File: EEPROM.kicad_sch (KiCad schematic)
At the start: 22 parts, among them IC1 PCA6408APW, IC2 AT24CS01, U2 TPS613221ADBVT

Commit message: Update signage
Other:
- moved on the sheet: C34, C37, C38, C39, D1, D2, D3, D4, IC1, IC2, L1, R10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

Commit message: [#45231] globlib
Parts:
- C34, C37: footprint lpddr4-testbed-footprints:0402-cap -> antmicro-footprints:C_0402_1005Metric; symbol lpddr4-testbed:C_4u7_0402 -> antmicroCapacitors0402:C_4u7_0402
- C38, C39: footprint lpddr4-testbed-footprints:0402-cap -> antmicro-footprints:C_0402_1005Metric; symbol lpddr4-testbed:C_100n_0402 -> antmicroCapacitors0402:C_100n_0402
- R10, R11, R12, R9: footprint lpddr4-testbed-footprints:0402-res -> antmicro-footprints:R_0402_1005Metric; symbol lpddr4-testbed:R_220R_0402 -> antmicroResistors0402:R_220R_0402
- R13, R14: footprint lpddr4-testbed-footprints:0402-res -> antmicro-footprints:R_0402_1005Metric; symbol lpddr4-testbed:R_10k_0402 -> antmicroResistors0402:R_10k_0402
- R8: footprint lpddr4-testbed-footprints:0402-res -> antmicro-footprints:R_0402_1005Metric; symbol lpddr4-testbed:R_0R_0402 -> antmicroResistors0402:R_0R_0402
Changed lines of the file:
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@@
     )
   )
-  (symbol (lib_id "lpddr4-testbed:C_4u7_0402") (at 189.865 91.44 0) (unit 1)
+  (symbol (lib_id "antmicroCapacitors0402:C_4u7_0402") (at 189.865 91.44 0) (unit 1)
     (in_bom yes) (on_board yes)
     (property "Reference" "C34" (id 0) (at 192.786 90.297 0)
@@
       (effects (font (size 1.524 1.524)) hide)
     )
-    (property "Footprint" "lpddr4-testbed-footprints:0402-cap" (id 2) (at 194.945 86.36 0)
+    (property "Footprint" "antmicro-footprints:C_0402_1005Metric" (id 2) (at 194.945 86.36 0)
       (effects (font (size 1.524 1.524)) (justify left) hide)
     )
@@
     (pin "2")
   )
-  (symbol (lib_id "lpddr4-testbed:C_4u7_0402") (at 235.585 91.44 0) (unit 1)
+  (symbol (lib_id "antmicroCapacitors0402:C_4u7_0402") (at 235.585 91.44 0) (unit 1)
     (in_bom yes) (on_board yes)
     (property "Reference" "C37" (id 0) (at 238.506 90.297 0)
@@
       (effects (font (size 1.524 1.524)) hide)
     )
-    (property "Footprint" "lpddr4-testbed-footprints:0402-cap" (id 2) (at 240.665 86.36 0)
+    (property "Footprint" "antmicro-footprints:C_0402_1005Metric" (id 2) (at 240.665 86.36 0)
       (effects (font (size 1.524 1.524)) (justify left) hide)
     )
@@
     (pin "5")
   )
-  (symbol (lib_id "lpddr4-testbed:R_0R_0402") (at 212.725 76.2 0) (unit 1)
+  (symbol (lib_id "antmicroResistors0402:R_0R_0402") (at 212.725 76.2 0) (unit 1)
     (in_bom yes) (on_board yes)
     (property "Reference" "R8" (id 0) (at 212.725 71.12 0)
@@
       (effects (font (size 1.524 1.524)) hide)
     )
-    (property "Footprint" "lpddr4-testbed-footprints:0402-res" (id 2) (at 217.805 71.12 0)
+    (property "Footprint" "antmicro-footprints:R_0402_1005Metric" (id 2) (at 217.805 71.12 0)
       (effects (font (size 1.524 1.524)) (justify left) hide)
     )
@@
     (pin "2")
   )
-  (symbol (lib_id "lpddr4-testbed:GND") (at 189.865 95.25 0) (unit 1)
+  (symbol (lib_id "antmicropower:GND") (at 189.865 95.25 0) (unit 1)
     (in_bom yes) (on_board yes)
     (property "Reference" "#PWR0106" (id 0) (at 189.865 101.6 0)
@@
     (pin "1")
   )
-  (symbol (lib_id "lpddr4-testbed:GND") (at 235.585 95.25 0) (unit 1)
+  (symbol (lib_id "antmicropower:GND") (at 235.585 95.25 0) (unit 1)
     (in_bom yes) (on_board yes)
     (property "Reference" "#PWR0107" (id 0) (at 235.585 101.6 0)
@@
     (pin "1")
   )
-  (symbol (lib_id "lpddr4-testbed:GND") (at 230.505 95.25 0) (unit 1)
+  (symbol (lib_id "antmicropower:GND") (at 230.505 95.25 0) (unit 1)
     (in_bom yes) (on_board yes)
     (property "Reference" "#PWR0108" (id 0) (at 230.505 101.6 0)
@@
     (pin "1")
   )
-  (symbol (lib_id "lpddr4-testbed:R_10k_0402") (at 188.595 175.26 270) (unit 1)
+  (symbol (lib_id "antmicroResistors0402:R_10k_0402") (at 188.595 175.26 270) (unit 1)
     (in_bom yes) (on_board yes)
     (property "Reference" "R13" (id 0) (at 190.373 174.117 90)
@@
       (effects (font (size 1.524 1.524)) hide)
     )
-    (property "Footprint" "lpddr4-testbed-footprints:0402-res" (id 2) (at 193.675 180.34 0)
+    (property "Footprint" "antmicro-footprints:R_0402_1005Metric" (id 2) (at 193.675 180.34 0)
       (effects (font (size 1.524 1.524)) (justify left) hide)
     )
@@
     (pin "2")
   )
-  (symbol (lib_id "lpddr4-testbed:R_220R_0402") (at 248.285 120.65 0) (unit 1)
+  (symbol (lib_id "antmicroResistors0402:R_220R_0402") (at 248.285 120.65 0) (unit 1)
     (in_bom yes) (on_board yes)
     (property "Reference" "R9" (id 0) (at 243.205 119.38 0)
@@
       (effects (font (size 1.524 1.524)) hide)
     )
-    (property "Footprint" "lpddr4-testbed-footprints:0402-res" (id 2) (at 253.365 115.57 0)
+    (property "Footprint" "antmicro-footprints:R_0402_1005Metric" (id 2) (at 253.365 115.57 0)
       (effects (font (size 1.524 1.524)) (justify left) hide)
     )
@@
     (pin "2")
   )
-  (symbol (lib_id "lpddr4-testbed:R_220R_0402") (at 248.285 123.19 0) (unit 1)
+  (symbol (lib_id "antmicroResistors0402:R_220R_0402") (at 248.285 123.19 0) (unit 1)
     (in_bom yes) (on_board yes)
     (property "Reference" "R10" (id 0) (at 243.205 121.92 0)
@@
       (effects (font (size 1.524 1.524)) hide)
     )
-    (property "Footprint" "lpddr4-testbed-footprints:0402-res" (id 2) (at 253.365 118.11 0)
+    (property "Footprint" "antmicro-footprints:R_0402_1005Metric" (id 2) (at 253.365 118.11 0)
       (effects (font (size 1.524 1.524)) (justify left) hide)
     )
@@
     (pin "2")
   )
-  (symbol (lib_id "lpddr4-testbed:R_220R_0402") (at 248.285 125.73 0) (unit 1)
+  (symbol (lib_id "antmicroResistors0402:R_220R_0402") (at 248.285 125.73 0) (unit 1)
     (in_bom yes) (on_board yes)
     (property "Reference" "R11" (id 0) (at 243.205 124.46 0)
@@
       (effects (font (size 1.524 1.524)) hide)
     )
-    (property "Footprint" "lpddr4-testbed-footprints:0402-res" (id 2) (at 253.365 120.65 0)
+    (property "Footprint" "antmicro-footprints:R_0402_1005Metric" (id 2) (at 253.365 120.65 0)
       (effects (font (size 1.524 1.524)) (justify left) hide)
     )
@@
     (pin "2")
   )
-  (symbol (lib_id "lpddr4-testbed:R_220R_0402") (at 248.285 128.27 0) (unit 1)
+  (symbol (lib_id "antmicroResistors0402:R_220R_0402") (at 248.285 128.27 0) (unit 1)
     (in_bom yes) (on_board yes)
     (property "Reference" "R12" (id 0) (at 243.205 127 0)
@@
       (effects (font (size 1.524 1.524)) hide)
     )
-    (property "Footprint" "lpddr4-testbed-footprints:0402-res" (id 2) (at 253.365 123.19 0)
+    (property "Footprint" "antmicro-footprints:R_0402_1005Metric" (id 2) (at 253.365 123.19 0)
       (effects (font (size 1.524 1.524)) (justify left) hide)
     )
@@
     (pin "2")
   )
-  (symbol (lib_id "lpddr4-testbed:C_100n_0402") (at 253.365 182.88 0) (unit 1)
+  (symbol (lib_id "antmicroCapacitors0402:C_100n_0402") (at 253.365 182.88 0) (unit 1)
     (in_bom yes) (on_board yes)
     (property "Reference" "C38" (id 0) (at 256.286 181.737 0)
@@
       (effects (font (size 1.524 1.524)) hide)
     )
-    (property "Footprint" "lpddr4-testbed-footprints:0402-cap" (id 2) (at 258.445 177.8 0)
+    (property "Footprint" "antmicro-footprints:C_0402_1005Metric" (id 2) (at 258.445 177.8 0)
       (effects (font (size 1.524 1.524)) (justify left) hide)
     )
@@
     (pin "2")
   )
-  (symbol (lib_id "lpddr4-testbed:GND") (at 258.445 153.67 0) (unit 1)
+  (symbol (lib_id "antmicropower:GND") (at 258.445 153.67 0) (unit 1)
     (in_bom yes) (on_board yes)
     (property "Reference" "#PWR0109" (id 0) (at 258.445 160.02 0)
@@
     (pin "1")
   )
-  (symbol (lib_id "lpddr4-testbed:GND") (at 266.065 153.67 0) (unit 1)
+  (symbol (lib_id "antmicropower:GND") (at 266.065 153.67 0) (unit 1)
     (in_bom yes) (on_board yes)
     (property "Reference" "#PWR0110" (id 0) (at 266.065 160.02 0)
@@
     (pin "1")
   )
-  (symbol (lib_id "lpddr4-testbed:GND") (at 273.685 153.67 0) (unit 1)
+  (symbol (lib_id "antmicropower:GND") (at 273.685 153.67 0) (unit 1)
     (in_bom yes) (on_board yes)
     (property "Reference" "#PWR0111" (id 0) (at 273.685 160.02 0)
@@
     (pin "1")
   )
-  (symbol (lib_id "lpddr4-testbed:GND") (at 281.305 153.67 0) (unit 1)
+  (symbol (lib_id "antmicropower:GND") (at 281.305 153.67 0) (unit 1)
     (in_bom yes) (on_board yes)
     (property "Reference" "#PWR0112" (id 0) (at 281.305 160.02 0)
@@
     (pin "1")
   )
-  (symbol (lib_id "lpddr4-testbed:GND") (at 198.755 152.4 0) (unit 1)
+  (symbol (lib_id "antmicropower:GND") (at 198.755 152.4 0) (unit 1)
     (in_bom yes) (on_board yes)
     (property "Reference" "#PWR0113" (id 0) (at 198.755 158.75 0)
@@
     (pin "5")
   )
-  (symbol (lib_id "lpddr4-testbed:R_10k_0402") (at 196.215 175.26 270) (unit 1)
+  (symbol (lib_id "antmicroResistors0402:R_10k_0402") (at 196.215 175.26 270) (unit 1)
     (in_bom yes) (on_board yes)
     (property "Reference" "R14" (id 0) (at 197.993 174.117 90)
@@
       (effects (font (size 1.524 1.524)) hide)
     )
-    (property "Footprint" "lpddr4-testbed-footprints:0402-res" (id 2) (at 201.295 180.34 0)
+    (property "Footprint" "antmicro-footprints:R_0402_1005Metric" (id 2) (at 201.295 180.34 0)
       (effects (font (size 1.524 1.524)) (justify left) hide)
     )
@@
     (pin "2")
   )
-  (symbol (lib_id "lpddr4-testbed:GND") (at 196.215 190.5 0) (unit 1)
+  (symbol (lib_id "antmicropower:GND") (at 196.215 190.5 0) (unit 1)
     (in_bom yes) (on_board yes)
     (property "Reference" "#PWR0114" (id 0) (at 196.215 196.85 0)
@@
     (pin "1")
   )
-  (symbol (lib_id "lpddr4-testbed:GND") (at 231.775 190.5 0) (unit 1)
+  (symbol (lib_id "antmicropower:GND") (at 231.775 190.5 0) (unit 1)
     (in_bom yes) (on_board yes)
     (property "Reference" "#PWR0115" (id 0) (at 231.775 196.85 0)
@@
     (pin "1")
   )
-  (symbol (lib_id "lpddr4-testbed:GND") (at 253.365 190.5 0) (unit 1)
+  (symbol (lib_id "antmicropower:GND") (at 253.365 190.5 0) (unit 1)
     (in_bom yes) (on_board yes)
     (property "Reference" "#PWR0116" (id 0) (at 253.365 196.85 0)
@@
     (pin "1")
   )
-  (symbol (lib_id "lpddr4-testbed:C_100n_0402") (at 266.065 182.88 0) (unit 1)
+  (symbol (lib_id "antmicroCapacitors0402:C_100n_0402") (at 266.065 182.88 0) (unit 1)
     (in_bom yes) (on_board yes)
     (property "Reference" "C39" (id 0) (at 268.986 181.737 0)
@@
       (effects (font (size 1.524 1.524)) hide)
     )
-    (property "Footprint" "lpddr4-testbed-footprints:0402-cap" (id 2) (at 271.145 177.8 0)
+    (property "Footprint" "antmicro-footprints:C_0402_1005Metric" (id 2) (at 271.145 177.8 0)
       (effects (font (size 1.524 1.524)) (justify left) hide)
     )
@@
     (pin "2")
   )
-  (symbol (lib_id "lpddr4-testbed:GND") (at 266.065 190.5 0) (unit 1)
+  (symbol (lib_id "antmicropower:GND") (at 266.065 190.5 0) (unit 1)
     (in_bom yes) (on_board yes)
     (property "Reference" "#PWR0117" (id 0) (at 266.065 196.85 0)

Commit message: Fix missing global links (wip), designators fixed
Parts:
- removed D1, D2, D3, D4: KP-1608CGCK, lpddr4-testbed-footprints:LED_0603, symbol lpddr4-testbed:KP-1608CGCK
- removed IC1: PCA6408APW, lpddr4-testbed-footprints:TSSOP-16, symbol lpddr4-testbed:PCA6408APW
- removed IC2: AT24CS01, lpddr4-testbed-footprints:SOT-23-5, symbol lpddr4-testbed:AT24CS01-antmicroMemory
- removed TP1, TP2, TP3: TP_SMD1MM, lpddr4-testbed-footprints:Testpoint_smd_1mm, symbol lpddr4-testbed:TP_SMD1MM
- added D1, D2, D3, D4: LED_G_0603_KP-1608CGCK, antmicro-footprints:LED_0603_1608Metric_G, symbol antmicroLEDIndicationDiscrete:LED_G_0603_KP-1608CGCK
- added IC1: PCA6408A_TSSOP, antmicro-footprints:TSSOP-16_4.4x5mm_P0.65mm, symbol antmicroInterfaceIOExpanders:PCA6408A_TSSOP
- added IC2: AT24CS01_SOT23, antmicro-footprints:SOT-23-5, symbol antmicroMemory:AT24CS01_SOT23
- added TP1, TP2, TP3: TP_0.75mm_SMD, antmicro-footprints:TP_SMD_0.75mm, symbol antmicroTestPoints:TP_0.75mm_SMD
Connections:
- net GND: now also D1.2, D2.2, D3.2, D4.2, IC1.8 (GND), IC2.2 (GND), IC2.5 (WP), TP3.1
- net SCL: now also IC1.14 (SCL), IC2.1 (SCL)
- net SDA: now also IC1.15 (SDA), IC2.3 (SDA)
- net VDD1: now also IC1.1 (VDD(I2C)), IC1.2 (ADDR), IC1.3 (~{RESET}), IC2.4 (VCC)
- net VDDLED: now also IC1.16 (VDD(P))
- net at R9.1: now also IC1.4 (P0)
- net at R9.2: now also D1.1
- net at R10.1: now also IC1.5 (P1)
- net at R10.2: now also D2.1
- net at R11.1: now also IC1.6 (P2)
- net at R11.2: now also D3.1
- net at R12.2: now also D4.1
- net at R12.1: now also IC1.7 (P3)
- new net: IC1.9 (P4), TP1.1
- new net: IC1.10 (P5), TP2.1
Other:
- moved on the sheet: R10, R11, R12, R13, R14, R9

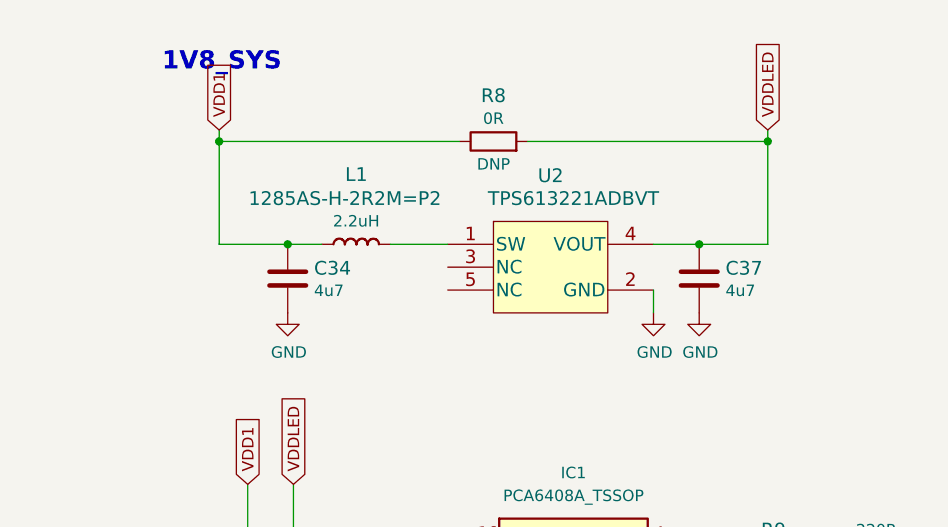
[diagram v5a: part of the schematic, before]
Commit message: Fix missing global links
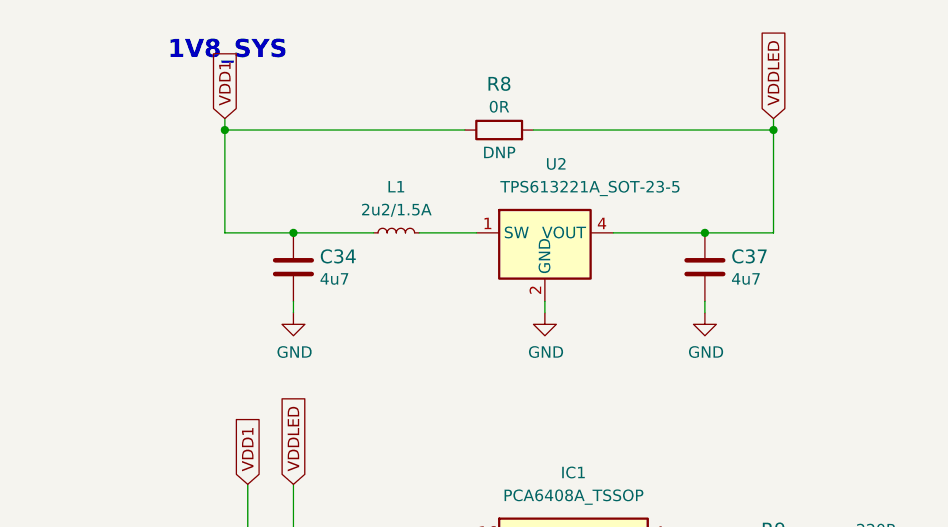
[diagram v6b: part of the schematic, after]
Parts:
- removed L1: 1285AS-H-2R2M=P2, lpddr4-testbed-footprints:0805-res, symbol lpddr4-testbed:1285AS-H-2R2M=P2
- removed U2: TPS613221ADBVT, lpddr4-testbed-footprints:SOT-23-5, symbol lpddr4-testbed:TPS613221ADBVT-antmicroDCDCConverters
- added L1: L_2u2_1.5A_1285AS-H, antmicro-footprints:L_0806_2016Metric, symbol antmicroFixedInductors:L_2u2_1.5A_1285AS-H
- added U2: TPS613221A_SOT-23-5, antmicro-footprints:SOT-23-5, symbol antmicroDCDCConverters:TPS613221A_SOT-23-5
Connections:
- net GND: now also U2.2 (GND)
- net VDD1: now also L1.1
- net VDDLED: now also U2.4 (VOUT)
- new net: L1.2, U2.1 (SW)
- new net: U2.3 (NC), U2.5 (NC)
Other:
- moved on the sheet: C34, C37, R8
